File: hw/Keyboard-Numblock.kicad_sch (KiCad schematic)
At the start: 18 parts, among them X2000 Mounting-Hole-M3, X2001 Mounting-Hole-M3, X2002 Mounting-Hole-M3, X2003 Mounting-Hole-M3, X2004 Distance-Bolt_M3x5, X2005 Distance-Bolt_M3x5, X2006 Distance-Bolt_M3x5, X2007 Distance-Bolt_M3x5, X2008 Screw M3x10, X2009 Screw M3x10, X2010 Screw M3x10, X2011 Screw M3x10, X2012 Screw M3x10, X2013 Screw M3x10, X2014 Screw M3x10, X2015 Screw M3x10

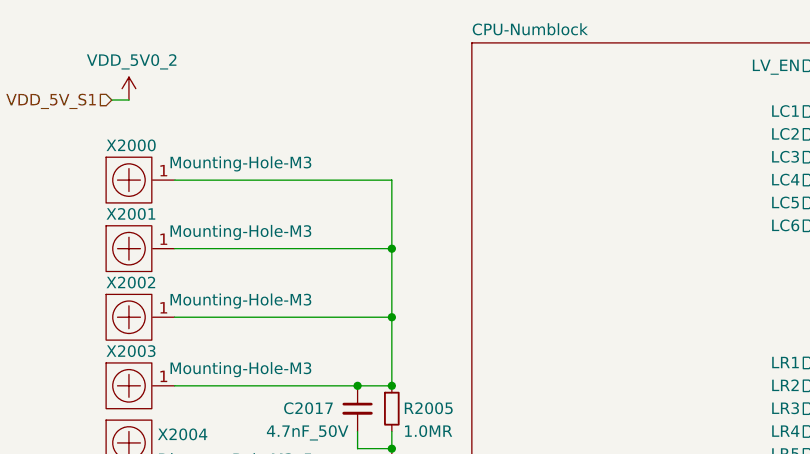
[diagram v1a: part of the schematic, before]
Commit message: Update schematic:
- Add ESD protection.
- Adjust distance bolts so they fit to the MX mounting plate.
- Make key layout symmetric.
- Add resistor to TX driver outputs.
- Use alternate IO functions on inter-board connectors.
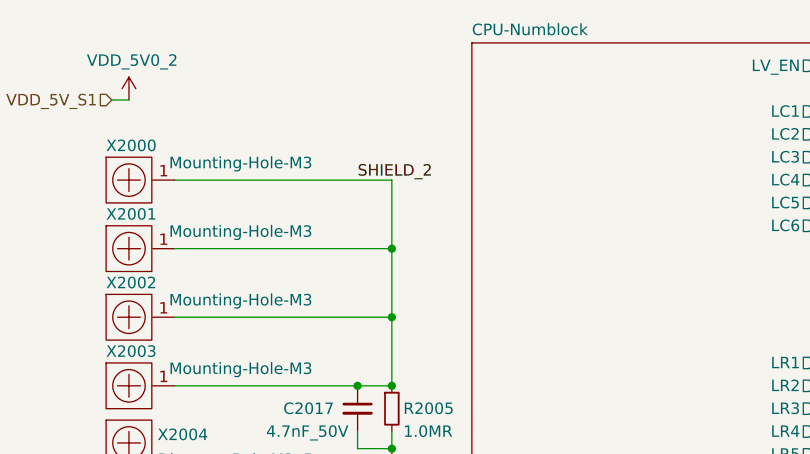
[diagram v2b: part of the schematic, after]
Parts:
- X2004, X2005, X2006, X2007: footprint Keyboard:DistanceBolt-M3x5 -> Keyboard:DistanceBolt-6x3.5; symbol Keyboard:Distance-Bolt_M3x5 -> Keyboard:Distance-Bolt_6x3.5
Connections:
- net SHIELD_2: now reaches C2017.1, R2005.1, X2000.1, X2001.1, X2002.1, X2003.1
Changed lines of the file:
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@@
+    (effects (font (size 1.27 1.27)) (justify left bottom))
+  )
+  (label "SHIELD_2" (at 63.5 40.64 0)
     (effects (font (size 1.27 1.27)) (justify left bottom))
   )
@@
     (pin "2")
   )
-  (symbol (lib_id "Keyboard:Distance-Bolt_M3x5") (at 38.1 82.55 0) (unit 1)
+  (symbol (lib_id "Keyboard:Distance-Bolt_6x3.5") (at 38.1 82.55 0) (unit 1)
     (in_bom yes) (on_board yes) (fields_autoplaced)
     (property "Reference" "X2006" (id 0) (at 41.275 81.6415 0)
@@
       (effects (font (size 1.27 1.27)) (justify left))
     )
-    (property "Footprint" "Keyboard:DistanceBolt-M3x5" (id 2) (at 38.1 82.55 0)
+    (property "Footprint" "Keyboard:DistanceBolt-6x3.5" (id 2) (at 38.1 82.55 0)
       (effects (font (size 1.27 1.27)) hide)
     )
@@
     )
   )
-  (symbol (lib_id "Keyboard:Distance-Bolt_M3x5") (at 38.1 88.9 0) (unit 1)
+  (symbol (lib_id "Keyboard:Distance-Bolt_6x3.5") (at 38.1 88.9 0) (unit 1)
     (in_bom yes) (on_board yes) (fields_autoplaced)
     (property "Reference" "X2007" (id 0) (at 41.275 87.9915 0)
@@
       (effects (font (size 1.27 1.27)) (justify left))
     )
-    (property "Footprint" "Keyboard:DistanceBolt-M3x5" (id 2) (at 38.1 88.9 0)
+    (property "Footprint" "Keyboard:DistanceBolt-6x3.5" (id 2) (at 38.1 88.9 0)
       (effects (font (size 1.27 1.27)) hide)
     )
@@
     )
   )
-  (symbol (lib_id "Keyboard:Distance-Bolt_M3x5") (at 38.1 69.85 0) (unit 1)
+  (symbol (lib_id "Keyboard:Distance-Bolt_6x3.5") (at 38.1 69.85 0) (unit 1)
     (in_bom yes) (on_board yes) (fields_autoplaced)
     (property "Reference" "X2004" (id 0) (at 41.275 68.9415 0)
@@
       (effects (font (size 1.27 1.27)) (justify left))
     )
-    (property "Footprint" "Keyboard:DistanceBolt-M3x5" (id 2) (at 38.1 69.85 0)
+    (property "Footprint" "Keyboard:DistanceBolt-6x3.5" (id 2) (at 38.1 69.85 0)
       (effects (font (size 1.27 1.27)) hide)
     )
@@
     (pin "1")
   )
-  (symbol (lib_id "Keyboard:Distance-Bolt_M3x5") (at 38.1 76.2 0) (unit 1)
+  (symbol (lib_id "Keyboard:Distance-Bolt_6x3.5") (at 38.1 76.2 0) (unit 1)
     (in_bom yes) (on_board yes) (fields_autoplaced)
     (property "Reference" "X2005" (id 0) (at 41.275 75.2915 0)
@@
       (effects (font (size 1.27 1.27)) (justify left))
     )
-    (property "Footprint" "Keyboard:DistanceBolt-M3x5" (id 2) (at 38.1 76.2 0)
-      (effects (font (size 1.27 1.27)) hide)
-    )
+    (property "Footprint" "Keyboard:DistanceBolt-6x3.5" (id 2) (at 38.1 76.2 0)
+      (effects (font (size 1.27 1.27)) hide)
+    )
